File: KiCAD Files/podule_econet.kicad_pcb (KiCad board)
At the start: 2 copper layers, 160 x 100 mm, 83 parts, among them IC1 68B54, IC10 SST39SF040, IC11 74HCT273, IC12 74HCT245, IC13 74HCT139, IC14 74HCT139, IC15 ATTINY45, IC2 74HCT132, IC3 74LS123, IC5 LM319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

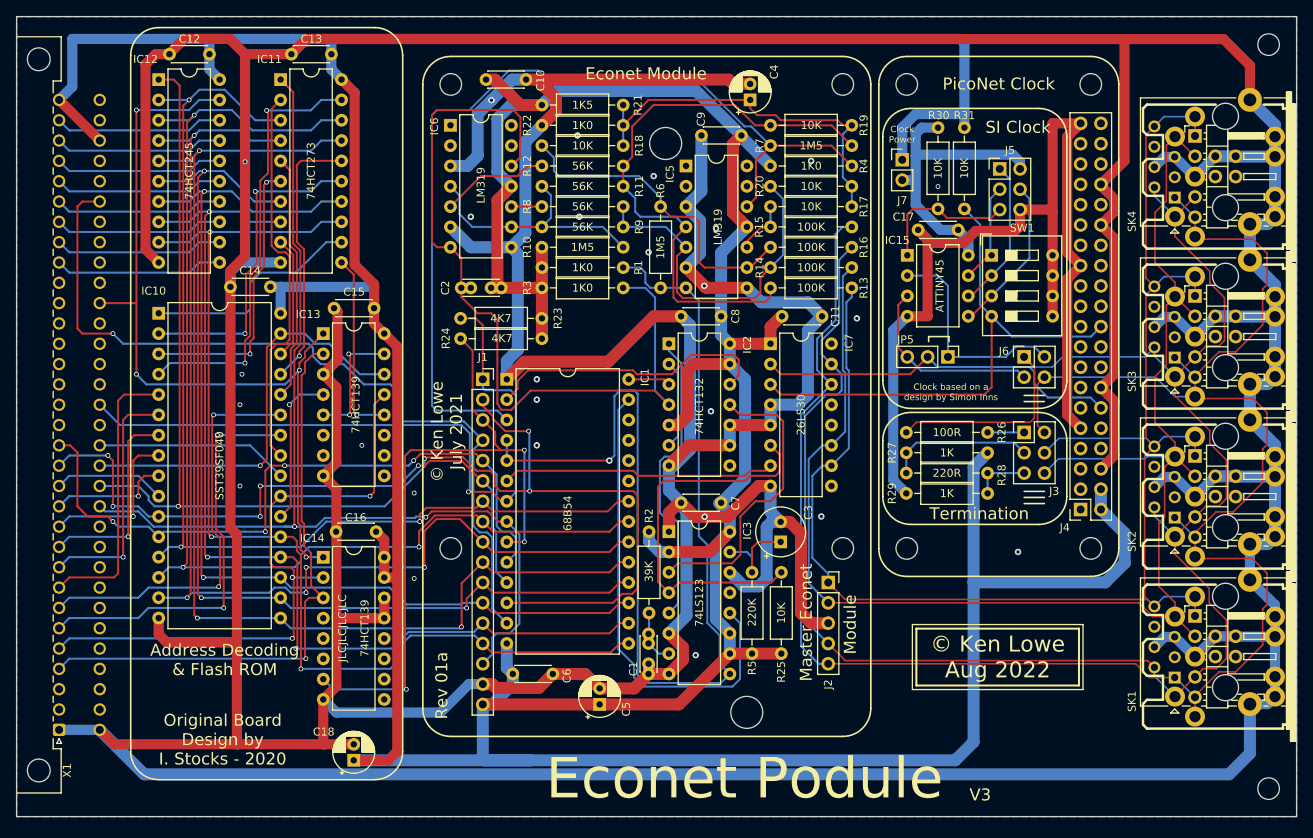
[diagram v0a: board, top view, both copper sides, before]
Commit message: Updated for KiCAD V9
+ Updated 3D model file locations
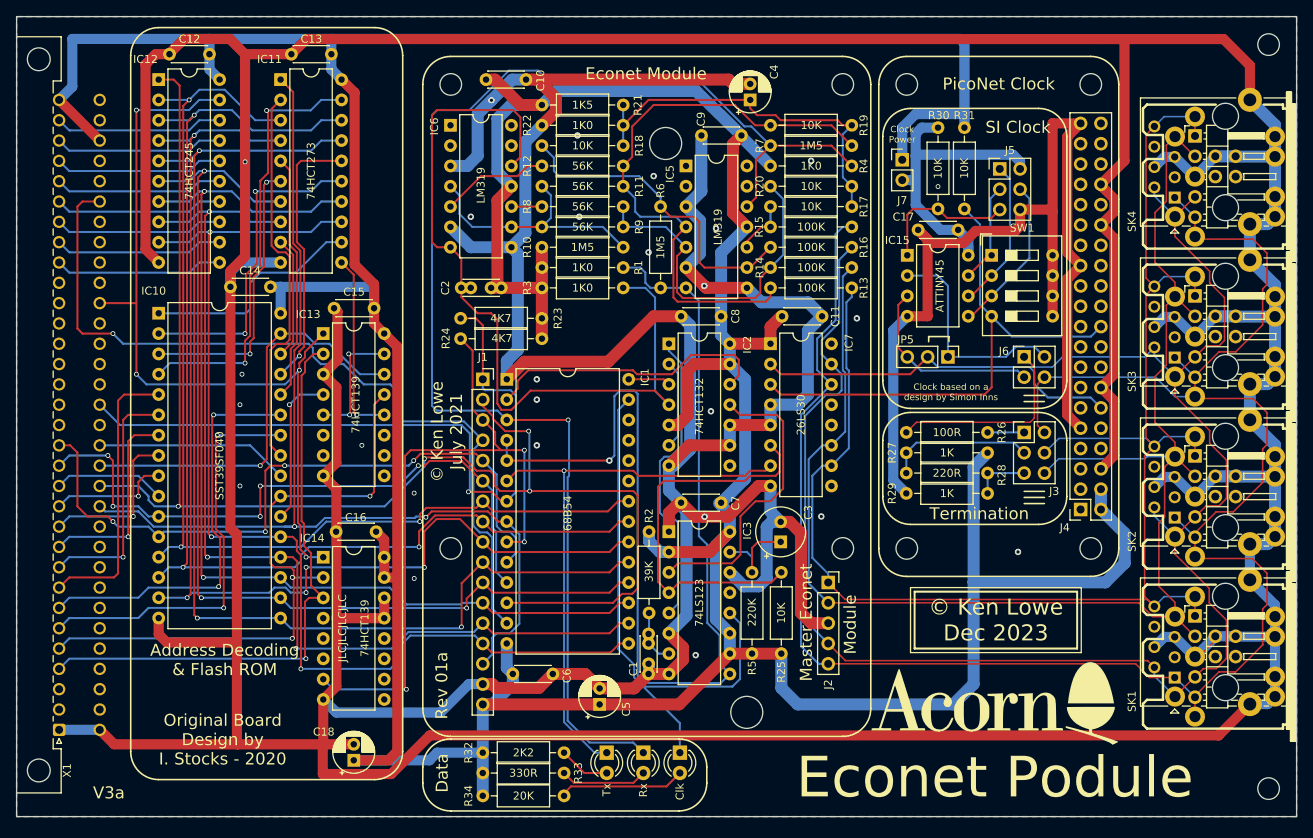
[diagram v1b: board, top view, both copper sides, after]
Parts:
- added G1: LOGO, EconetPodule:AcornLogo2, F.Cu at (190.0, 136.6)
- added LED1: Red, LED_THT:LED_D3.0mm, F.Cu at (141.1, 142.6)
- added LED2: Green, LED_THT:LED_D3.0mm, F.Cu at (145.7, 142.6)
- added LED3: Blue, LED_THT:LED_D3.0mm, F.Cu at (150.2, 142.6)
- added R32: 2K2, Resistor_THT:R_Axial_DIN0207_L6.3mm_D2.5mm_P10.16mm_Horizontal, F.Cu at (125.6, 142.6)
- added R33: 330R, Resistor_THT:R_Axial_DIN0207_L6.3mm_D2.5mm_P10.16mm_Horizontal, F.Cu at (125.6, 145.1)
- added R34: 20K, Resistor_THT:R_Axial_DIN0207_L6.3mm_D2.5mm_P10.16mm_Horizontal, F.Cu at (125.6, 148.0)
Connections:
- net Net-(IC1-Rx_Data) renamed /Rx_Data
- net Net-(IC1-Tx_Data) renamed /Tx_Data
- net Net-(IC1-~{DCD}) renamed /Econet_Clk
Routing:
- net /Rx_Data: track 115.0 -> 171.5 mm, vias 0 -> 1
- net +5V: track 685.6 -> 644.9 mm
- net /Tx_Data: track 34.3 -> 72.6 mm, vias 0 -> 1
- net GND: track 1234.9 -> 1204.9 mm
- net Net-(LED3-A): track 0.00 -> 15.5 mm
- net Net-(LED2-A): track 0.00 -> 10.9 mm
- net /Econet_Clk: track 59.0 -> 69.1 mm
- net Net-(LED1-A): track 0.00 -> 6.39 mm
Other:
- board text added: "Clk"
- board text added: "Data"
- board text added: "Rx"
- board text added: "Tx"
- board text added: "V3a"
- board text added: "© Ken Lowe Dec 2023"
- board text removed: "V3"
- board text removed: "© Ken Lowe Aug 2022"

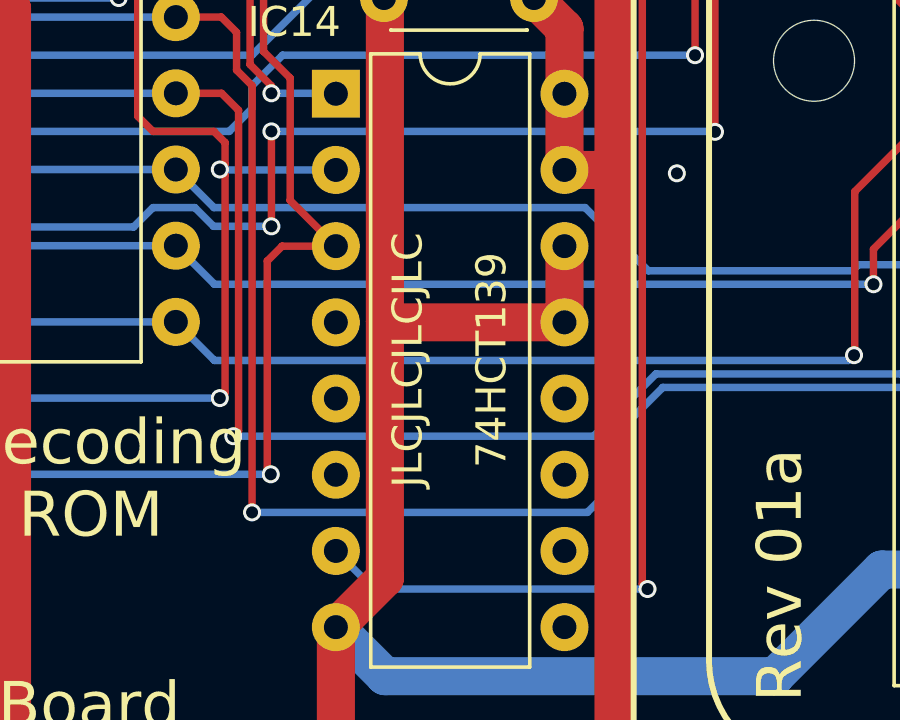
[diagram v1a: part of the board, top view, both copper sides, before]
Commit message: Remove JLC serial mark from PCB
Add 8x8mm box to rear of PCB for JLC 2D serial code instead.
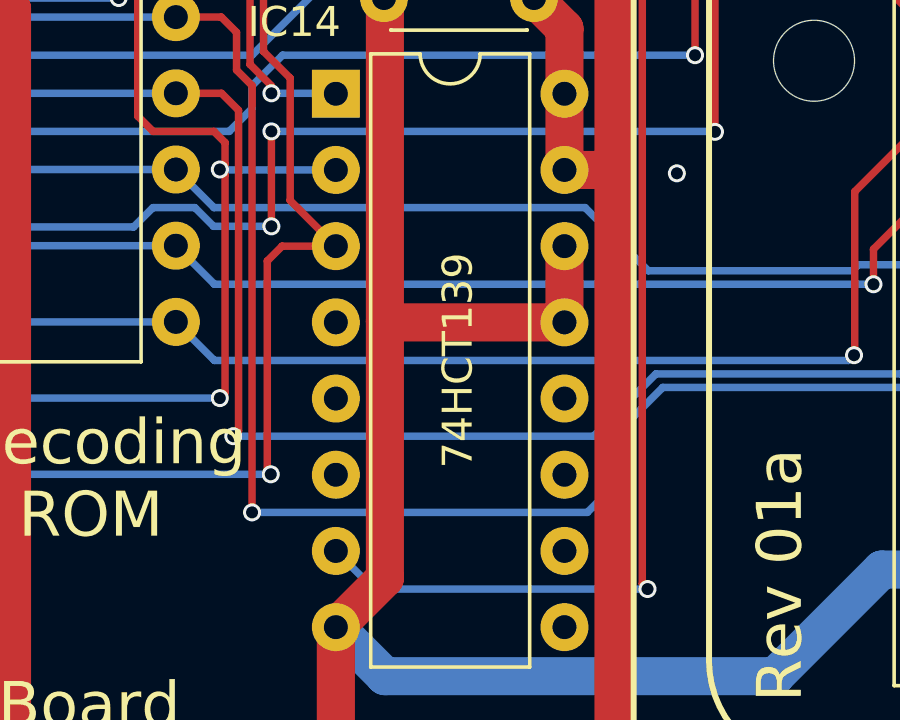
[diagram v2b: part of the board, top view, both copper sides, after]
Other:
- board text removed: "JLCJLCJLCJLC"
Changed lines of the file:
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@@
 		(grid_origin 223.83 147.046)
 		(pcbplotparams
-			(layerselection 0x00000000_00000000_55555555_555555f0)
+			(layerselection 0x00000000_00000000_55555555_5f55fff5)
 			(plot_on_all_layers_selection 0x00000000_00000000_00000000_00000000)
 			(disableapertmacros no)
@@
 			(crossoutdnponfab yes)
 			(subtractmaskfromsilk yes)
-			(outputformat 3)
+			(outputformat 1)
 			(mirror no)
 			(drillshape 0)
@@
 		)
 		(property "Value" "74HCT139"
-			(at 5.1865 8.875 90)
+			(at 4.064 8.89 90)
 			(layer "F.SilkS")
 			(effects
@@
 		(layer "B.SilkS")
 	)
+	(gr_rect
+		(start 196.83 136.046)
+		(end 204.83 144.046)
+		(stroke
+			(width 0.15)
+			(type solid)
+		)
+		(fill yes)
+		(layer "B.SilkS")
+	)
 	(gr_arc
 		(start 118.103 144.342)
@@
 		(layer "Edge.Cuts")
 	)
-	(gr_text "JLCJLCJLCJLC"
-		(at 108.0565 127 90)
-		(layer "F.SilkS")
-		(effects
-			(font
-				(size 1 1)
-				(thickness 0.15)
-			)
-		)
-	)
 	(gr_text "PicoNet Clock"
